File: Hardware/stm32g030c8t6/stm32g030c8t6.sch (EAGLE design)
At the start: 27 parts, among them IC1 STM32G030C8T6, IC2 AP2114HA-3.3TRG1, J1 USB_MINI-B_SMT, Y1 DSC6083CI1A-350K000T

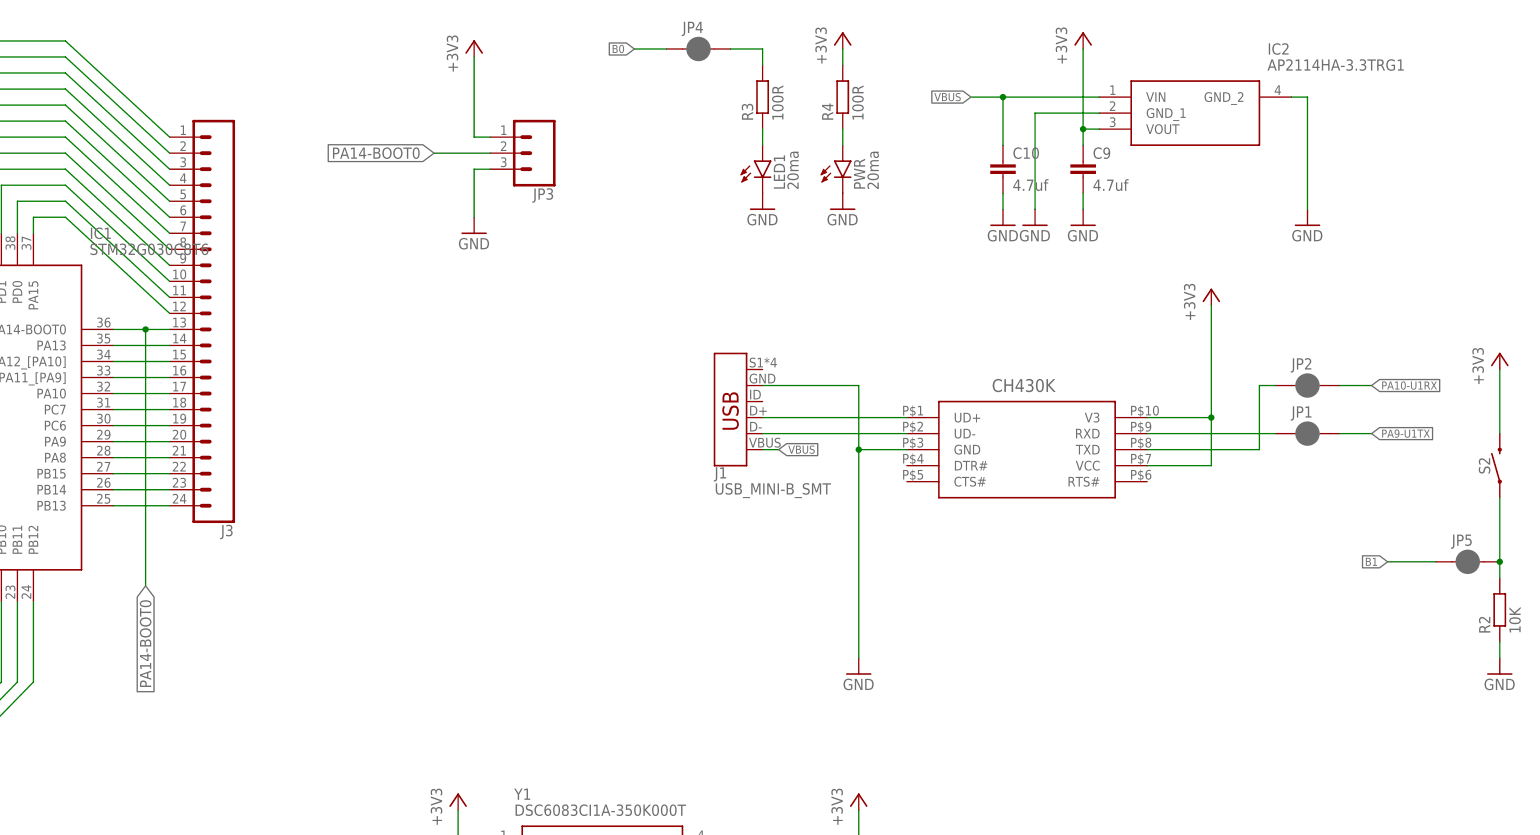
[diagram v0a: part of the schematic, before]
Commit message: Added pullup to RX pin
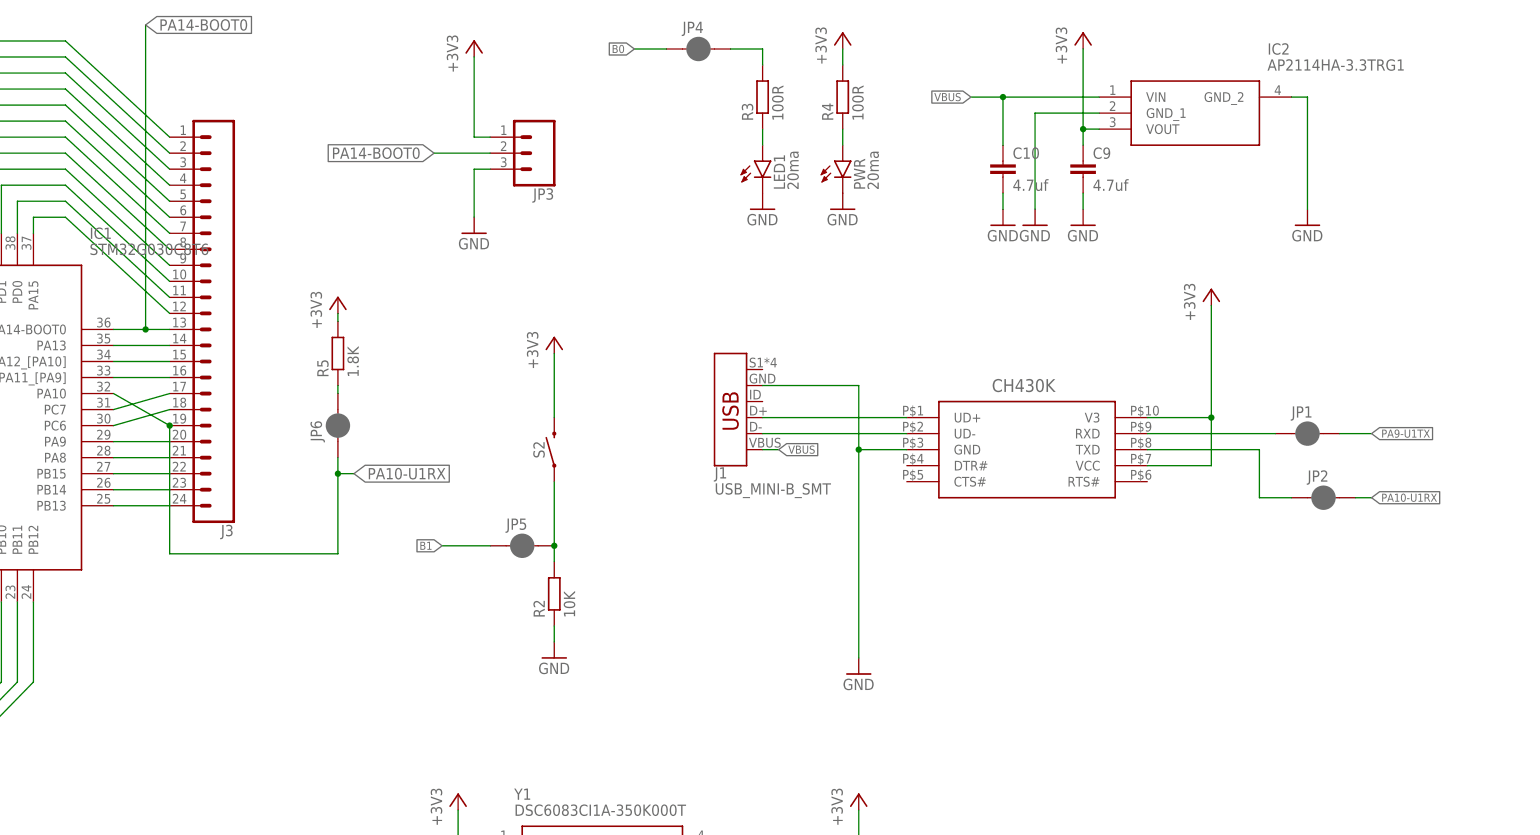
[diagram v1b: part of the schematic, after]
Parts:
- added JP6: JUMPER-SMT_2_NC_PASTE_SILK, SparkFun-Jumpers:JUMPER-SMT_2_NC_PASTE_SILK
- added R5: 1.8K, rcl:R-EU_R0805
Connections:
- new net N$1: JP6.2, R5.1
- net +3V3: now also R5.2
- net PA10-U1RX: now also J3.19, JP6.1; no longer J3.17
- net PC6: now also J3.18; no longer J3.19
- net PC7: now also J3.17; no longer J3.18
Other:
- moved on the sheet: JP2, JP5, R2, S2
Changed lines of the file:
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@@
 <part name="GND5" library="supply1" library_urn="urn:adsk.eagle:library:371" deviceset="GND" device=""/>
 <part name="GND6" library="supply1" library_urn="urn:adsk.eagle:library:371" deviceset="GND" device=""/>
+<part name="JP6" library="SparkFun-Jumpers" deviceset="JUMPER-SMT_2_NC_PASTE" device="_SILK" package3d_urn="urn:adsk.eagle:package:39282/1"/>
+<part name="+3V6" library="supply1" library_urn="urn:adsk.eagle:library:371" deviceset="+3V3" device=""/>
+<part name="R5" library="rcl" library_urn="urn:adsk.eagle:library:334" deviceset="R-EU_" device="R0805" package3d_urn="urn:adsk.eagle:package:23553/2" value="1.8K"/>
 </parts>
 <sheets>
@@
 <attribute name="NAME" x="267.97" y="54.61" size="1.778" layer="95" font="vector"/>
 </instance>
-<instance part="JP2" gate="G$1" x="270.51" y="59.69" smashed="yes">
-<attribute name="NAME" x="267.97" y="62.23" size="1.778" layer="95" font="vector"/>
+<instance part="JP2" gate="G$1" x="273.05" y="41.91" smashed="yes">
+<attribute name="NAME" x="270.51" y="44.45" size="1.778" layer="95" font="vector"/>
 </instance>
 <instance part="LED1" gate="G$1" x="184.15" y="95.25" smashed="yes">
@@
 <attribute name="NAME" x="171.45" y="115.57" size="1.778" layer="95" font="vector"/>
 </instance>
-<instance part="+3V8" gate="G$1" x="300.99" y="64.77" smashed="yes">
-<attribute name="VALUE" x="298.45" y="59.69" size="1.778" layer="96" rot="R90"/>
-</instance>
-<instance part="GND8" gate="1" x="300.99" y="13.97" smashed="yes">
-<attribute name="VALUE" x="298.45" y="11.43" size="1.778" layer="96"/>
-</instance>
-<instance part="JP5" gate="G$1" x="295.91" y="31.75" smashed="yes">
-<attribute name="NAME" x="293.37" y="34.29" size="1.778" layer="95" font="vector"/>
-</instance>
-<instance part="S2" gate="G$1" x="300.99" y="46.99" smashed="yes" rot="R90">
-<attribute name="NAME" x="299.466" y="46.99" size="1.778" layer="95" font="vector" rot="R90" align="bottom-center"/>
-</instance>
-<instance part="R2" gate="G$1" x="300.99" y="24.13" smashed="yes" rot="R90">
-<attribute name="NAME" x="299.4914" y="20.32" size="1.778" layer="95" rot="R90"/>
-<attribute name="VALUE" x="304.292" y="20.32" size="1.778" layer="96" rot="R90"/>
+<instance part="+3V8" gate="G$1" x="151.13" y="67.31" smashed="yes">
+<attribute name="VALUE" x="148.59" y="62.23" size="1.778" layer="96" rot="R90"/>
+</instance>
+<instance part="GND8" gate="1" x="151.13" y="16.51" smashed="yes">
+<attribute name="VALUE" x="148.59" y="13.97" size="1.778" layer="96"/>
+</instance>
+<instance part="JP5" gate="G$1" x="146.05" y="34.29" smashed="yes">
+<attribute name="NAME" x="143.51" y="36.83" size="1.778" layer="95" font="vector"/>
+</instance>
+<instance part="S2" gate="G$1" x="151.13" y="49.53" smashed="yes" rot="R90">
+<attribute name="NAME" x="149.606" y="49.53" size="1.778" layer="95" font="vector" rot="R90" align="bottom-center"/>
+</instance>
+<instance part="R2" gate="G$1" x="151.13" y="26.67" smashed="yes" rot="R90">
+<attribute name="NAME" x="149.6314" y="22.86" size="1.778" layer="95" rot="R90"/>
+<attribute name="VALUE" x="154.432" y="22.86" size="1.778" layer="96" rot="R90"/>
 </instance>
 <instance part="GND2" gate="1" x="-45.72" y="6.35" smashed="yes">
@@
 <instance part="GND6" gate="1" x="-10.16" y="6.35" smashed="yes">
 <attribute name="VALUE" x="-12.7" y="3.81" size="1.778" layer="96"/>
+</instance>
+<instance part="JP6" gate="G$1" x="116.84" y="53.34" smashed="yes" rot="R90">
+<attribute name="NAME" x="114.3" y="50.8" size="1.778" layer="95" font="vector" rot="R90"/>
+</instance>
+<instance part="+3V6" gate="G$1" x="116.84" y="73.66" smashed="yes">
+<attribute name="VALUE" x="114.3" y="68.58" size="1.778" layer="96" rot="R90"/>
+</instance>
+<instance part="R5" gate="G$1" x="116.84" y="64.77" smashed="yes" rot="R90">
+<attribute name="NAME" x="115.3414" y="60.96" size="1.778" layer="95" rot="R90"/>
+<attribute name="VALUE" x="120.142" y="60.96" size="1.778" layer="96" rot="R90"/>
 </instance>
 </instances>
@@
 <segment>
 <pinref part="GND8" gate="1" pin="GND"/>
-<wire x1="300.99" y1="19.05" x2="300.99" y2="16.51" width="0.1524" layer="91"/>
+<wire x1="151.13" y1="21.59" x2="151.13" y2="19.05" width="0.1524" layer="91"/>
 <pinref part="R2" gate="G$1" pin="1"/>
 </segment>
@@
 <pinref part="U$1" gate="G$1" pin="TXD"/>
 <wire x1="245.11" y1="49.53" x2="262.89" y2="49.53" width="0.1524" layer="91"/>
-<wire x1="262.89" y1="49.53" x2="262.89" y2="59.69" width="0.1524" layer="91"/>
-<wire x1="262.89" y1="59.69" x2="265.43" y2="59.69" width="0.1524" layer="91"/>
+<wire x1="262.89" y1="49.53" x2="262.89" y2="41.91" width="0.1524" layer="91"/>
+<wire x1="262.89" y1="41.91" x2="267.97" y2="41.91" width="0.1524" layer="91"/>
 <pinref part="JP2" gate="G$1" pin="1"/>
 </segment>
@@
 </segment>
 <segment>
-<wire x1="300.99" y1="52.07" x2="300.99" y2="62.23" width="0.1524" layer="91"/>
+<wire x1="151.13" y1="54.61" x2="151.13" y2="64.77" width="0.1524" layer="91"/>
 <pinref part="+3V8" gate="G$1" pin="+3V3"/>
 <pinref part="S2" gate="G$1" pin="2"/>
@@
 <pinref part="+3V4" gate="G$1" pin="+3V3"/>
 </segment>
+<segment>
+<pinref part="R5" gate="G$1" pin="2"/>
+<pinref part="+3V6" gate="G$1" pin="+3V3"/>
+<wire x1="116.84" y1="69.85" x2="116.84" y2="71.12" width="0.1524" layer="91"/>
+</segment>
 </net>
 <net name="PB5" class="0">
@@
 <net name="N$4" class="0">
 <segment>
-<wire x1="300.99" y1="41.91" x2="300.99" y2="31.75" width="0.1524" layer="91"/>
+<wire x1="151.13" y1="44.45" x2="151.13" y2="34.29" width="0.1524" layer="91"/>
 <pinref part="JP5" gate="G$1" pin="2"/>
-<wire x1="300.99" y1="31.75" x2="300.99" y2="29.21" width="0.1524" layer="91"/>
-<junction x="300.99" y="31.75"/>
+<wire x1="151.13" y1="34.29" x2="151.13" y2="31.75" width="0.1524" layer="91"/>
+<junction x="151.13" y="34.29"/>
 <pinref part="S2" gate="G$1" pin="1"/>
 <pinref part="R2" gate="G$1" pin="2"/>
@@
 </segment>
 </net>
-<net name="PC7" class="0">
-<segment>
-<pinref part="IC1" gate="G$1" pin="PC7"/>
-<wire x1="81.28" y1="55.88" x2="90.17" y2="55.88" width="0.1524" layer="91"/>
-<pinref part="J3" gate="G$1" pin="18"/>
-</segment>
-</net>
-<net name="PC6" class="0">
-<segment>
-<pinref part="IC1" gate="G$1" pin="PC6"/>
-<wire x1="81.28" y1="53.34" x2="90.17" y2="53.34" width="0.1524" layer="91"/>
-<pinref part="J3" gate="G$1" pin="19"/>
-</segment>
-</net>
 <net name="PB15" class="0">
 <segment>
@@
 <pinref part="IC1" gate="G$1" pin="PA14-BOOT0"/>
 <wire x1="81.28" y1="68.58" x2="86.36" y2="68.58" width="0.1524" layer="91"/>
-<wire x1="86.36" y1="68.58" x2="86.36" y2="27.94" width="0.1524" layer="91"/>
-<label x="86.36" y="27.94" size="1.778" layer="95" rot="R270" xref="yes"/>
+<wire x1="86.36" y1="68.58" x2="86.36" y2="116.84" width="0.1524" layer="91"/>
+<label x="86.36" y="116.84" size="1.778" layer="95" xref="yes"/>
 <pinref part="J3" gate="G$1" pin="13"/>
 <wire x1="86.36" y1="68.58" x2="90.17" y2="68.58" width="0.1524" layer="91"/>
@@
 <net name="PA10-U1RX" class="0">
 <segment>
+<pinref part="JP2" gate="G$1" pin="2"/>
+<wire x1="278.13" y1="41.91" x2="280.67" y2="41.91" width="0.1524" layer="91"/>
+<label x="280.67" y="41.91" size="1.27" layer="95" xref="yes"/>
+</segment>
+<segment>
 <pinref part="IC1" gate="G$1" pin="PA10"/>
-<wire x1="81.28" y1="58.42" x2="90.17" y2="58.42" width="0.1524" layer="91"/>
-<pinref part="J3" gate="G$1" pin="17"/>
-</segment>
-<segment>
-<pinref part="JP2" gate="G$1" pin="2"/>
-<wire x1="275.59" y1="59.69" x2="280.67" y2="59.69" width="0.1524" layer="91"/>
-<label x="280.67" y="59.69" size="1.27" layer="95" xref="yes"/>
+<pinref part="J3" gate="G$1" pin="19"/>
+<wire x1="81.28" y1="58.42" x2="90.17" y2="53.34" width="0.1524" layer="91"/>
+<wire x1="90.17" y1="53.34" x2="90.17" y2="33.02" width="0.1524" layer="91"/>
+<junction x="90.17" y="53.34"/>
+<wire x1="90.17" y1="33.02" x2="116.84" y2="33.02" width="0.1524" layer="91"/>
+<pinref part="JP6" gate="G$1" pin="1"/>
+<wire x1="116.84" y1="48.26" x2="116.84" y2="45.72" width="0.1524" layer="91"/>
+<wire x1="116.84" y1="45.72" x2="119.38" y2="45.72" width="0.1524" layer="91"/>
+<label x="119.38" y="45.72" size="1.778" layer="95" xref="yes"/>
+<wire x1="116.84" y1="33.02" x2="116.84" y2="45.72" width="0.1524" layer="91"/>
+<junction x="116.84" y="45.72"/>
 </segment>
 </net>
@@
 <segment>
 <pinref part="JP5" gate="G$1" pin="1"/>
-<wire x1="290.83" y1="31.75" x2="283.21" y2="31.75" width="0.1524" layer="91"/>
-<label x="283.21" y="31.75" size="1.27" layer="95" rot="R180" xref="yes"/>
+<wire x1="140.97" y1="34.29" x2="133.35" y2="34.29" width="0.1524" layer="91"/>
+<label x="133.35" y="34.29" size="1.27" layer="95" rot="R180" xref="yes"/>
 </segment>
 </net>
@@
 </segment>
 </net>
+<net name="N$1" class="0">
+<segment>
+<pinref part="JP6" gate="G$1" pin="2"/>
+<pinref part="R5" gate="G$1" pin="1"/>
+<wire x1="116.84" y1="58.42" x2="116.84" y2="59.69" width="0.1524" layer="91"/>
+</segment>
+</net>
+<net name="PC7" class="0">
+<segment>
+<pinref part="IC1" gate="G$1" pin="PC7"/>
+<pinref part="J3" gate="G$1" pin="17"/>
+<wire x1="81.28" y1="55.88" x2="90.17" y2="58.42" width="0.1524" layer="91"/>
+</segment>
+</net>
+<net name="PC6" class="0">
+<segment>
+<pinref part="IC1" gate="G$1" pin="PC6"/>
+<pinref part="J3" gate="G$1" pin="18"/>
+<wire x1="81.28" y1="53.34" x2="90.17" y2="55.88" width="0.1524" layer="91"/>
+</segment>
+</net>
